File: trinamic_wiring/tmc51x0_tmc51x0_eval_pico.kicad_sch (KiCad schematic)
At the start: 4 parts, among them M1 Stepper_Motor

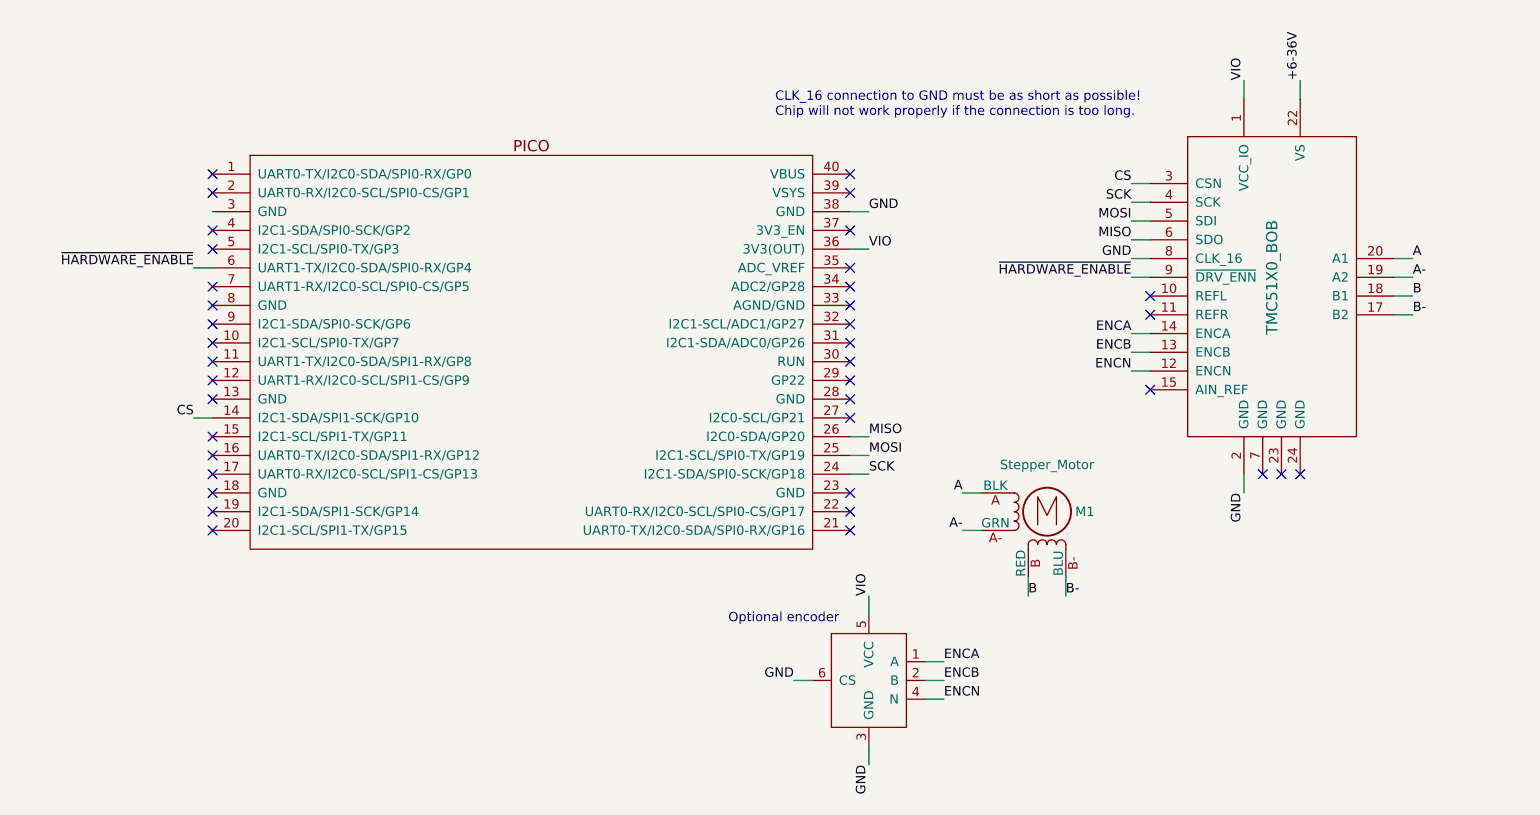
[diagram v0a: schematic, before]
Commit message: Add eval board
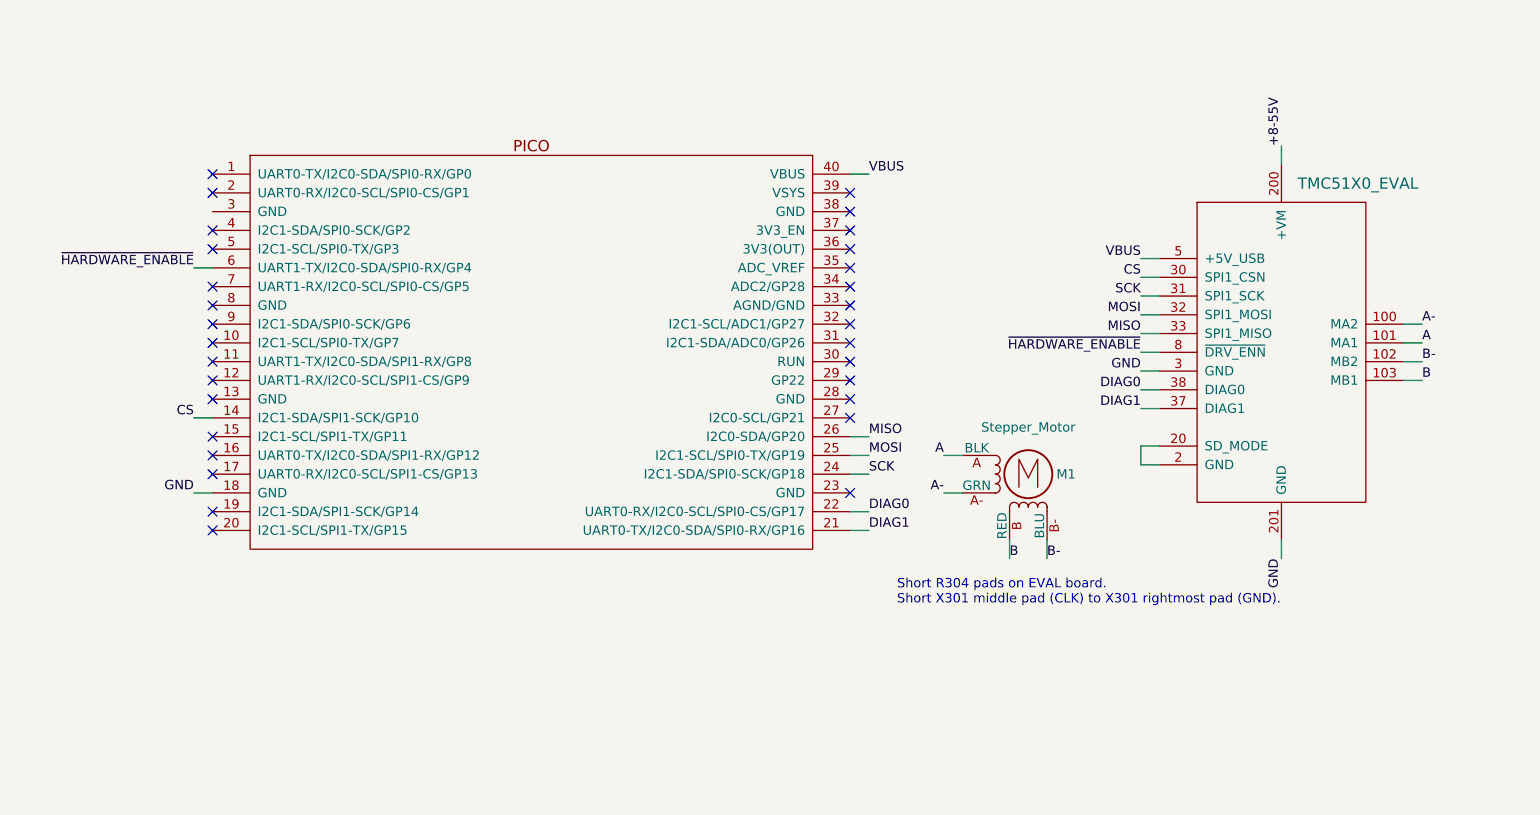
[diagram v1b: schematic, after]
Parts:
- removed BOB1: TMC51X0_BOB, symbol Janelia:TMC51X0_BOB
- removed ENC1: ENCODER_EMS22Q, symbol Janelia:ENCODER_EMS22Q
- added EVAL1: TMC51X0_EVAL, symbol Janelia:TMC51X0_EVAL
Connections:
- net A: now also EVAL1.101 (MA1)
- net A-: now also EVAL1.100 (MA2)
- net B: now also EVAL1.103 (MB1)
- net B-: now also EVAL1.102 (MB2)
- net CS: now also EVAL1.30 (SPI1_CSN)
- net GND: now also A3.18 (GND), EVAL1.201 (GND), EVAL1.3 (GND); no longer A3.38 (GND)
- net MISO: now also EVAL1.33 (SPI1_MISO)
- net MOSI: now also EVAL1.32 (SPI1_MOSI)
- net SCK: now also EVAL1.31 (SPI1_SCK)
- net ~{HARDWARE_ENABLE}: now also EVAL1.8 (~{DRV_ENN})
- net DIAG1: now reaches A3.21 (UART0-TX/I2C0-SDA/SPI0-RX/GP16)
- net DIAG1: now also EVAL1.37 (DIAG1)
- net DIAG0: now reaches A3.22 (UART0-RX/I2C0-SCL/SPI0-CS/GP17)
- net DIAG0: now also EVAL1.38 (DIAG0)
- net VBUS: now reaches A3.40 (VBUS)
- net VBUS: now also EVAL1.5 (+5V_USB)
- net VIO: no longer names the net of A3.36 (3V3(OUT))
- new net: EVAL1.2 (GND), EVAL1.20 (SD_MODE)
- new net +8-55V: EVAL1.200 (+VM)
- no-connect marks 38 -> 30
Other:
- note added: "Short R304 pads on EVAL board. Short X301 middle pad (CLK) to X301 rightmost pad (GND)."
- note removed: "CLK_16 connection to GND must be as short as possible! Chip will not work properly if the connection is too long."
- note removed: "Optional encoder"
- moved on the sheet: M1

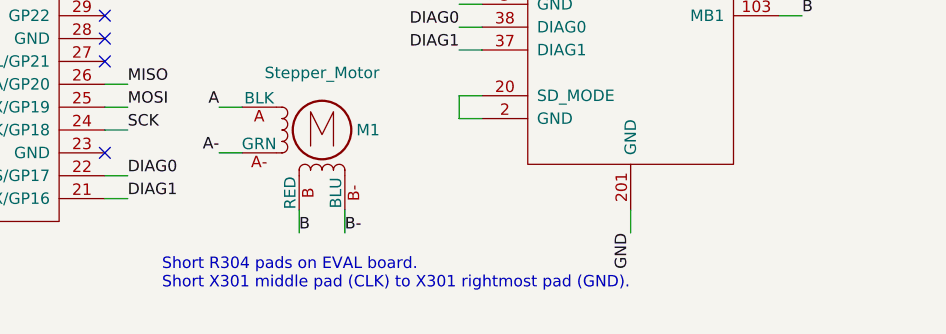
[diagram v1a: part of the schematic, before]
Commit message: Deleted sheet and updated comment on another
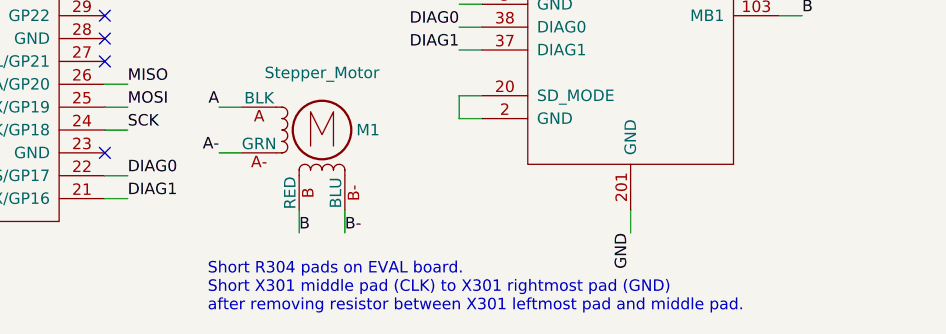
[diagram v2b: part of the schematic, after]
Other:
- note added: "Short R304 pads on EVAL board. Short X301 middle pad (CLK) to X301 rightmost pad (GND) after removing resistor between X301 leftmost pad and middle pad."
- note removed: "Short R304 pads on EVAL board. Short X301 middle pad (CLK) to X301 rightmost pad (GND)."
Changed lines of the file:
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@@
     (stroke (width 0) (type default))
   )
-  (text "Short R304 pads on EVAL board.\nShort X301 middle pad (CLK) to X301 rightmost pad (GND). "
-    (at 129.54 146.05 0)
+  (text "Short R304 pads on EVAL board.\nShort X301 middle pad (CLK) to X301 rightmost pad (GND)\nafter removing resistor between X301 leftmost pad and middle pad. "
+    (at 134.62 148.59 0)
     (effects (font (size 1.27 1.27)) (justify left bottom))
   )

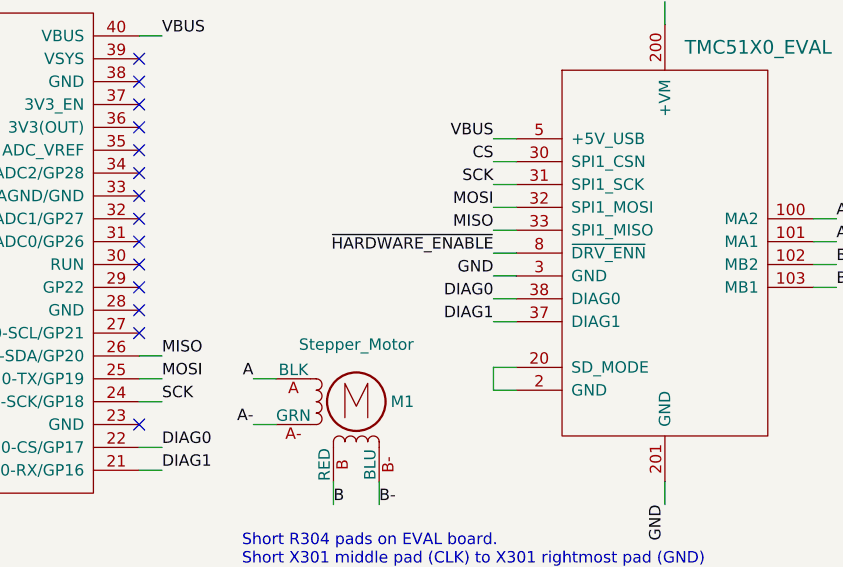
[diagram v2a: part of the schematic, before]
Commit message: miso -> cipo, mosi -> copi
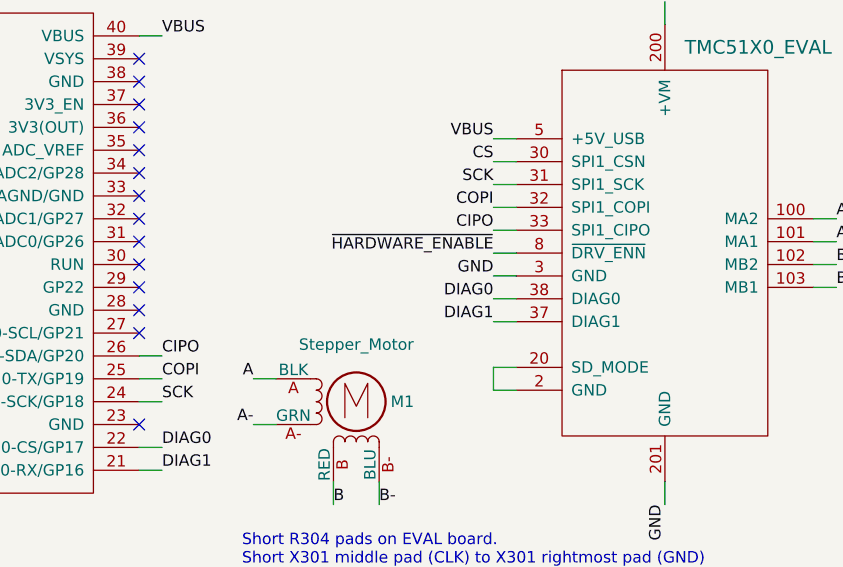
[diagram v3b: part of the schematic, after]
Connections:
- net MISO renamed CIPO
- net MOSI renamed COPI
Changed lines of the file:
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@@
     (effects (font (size 1.27 1.27)) (justify left bottom))
   )
-  (label "MISO" (at 162.56 109.22 180) (fields_autoplaced)
+  (label "CIPO" (at 162.56 109.22 180) (fields_autoplaced)
     (effects (font (size 1.27 1.27)) (justify right bottom))
   )
@@
     (effects (font (size 1.27 1.27)) (justify right bottom))
   )
-  (label "MOSI" (at 162.56 106.68 180) (fields_autoplaced)
+  (label "COPI" (at 162.56 106.68 180) (fields_autoplaced)
     (effects (font (size 1.27 1.27)) (justify right bottom))
   )
@@
     (effects (font (size 1.27 1.27)) (justify left bottom))
   )
-  (label "MISO" (at 125.73 123.19 0) (fields_autoplaced)
+  (label "CIPO" (at 125.73 123.19 0) (fields_autoplaced)
     (effects (font (size 1.27 1.27)) (justify left bottom))
   )
@@
     (effects (font (size 1.27 1.27)) (justify right bottom))
   )
-  (label "MOSI" (at 125.73 125.73 0) (fields_autoplaced)
+  (label "COPI" (at 125.73 125.73 0) (fields_autoplaced)
     (effects (font (size 1.27 1.27)) (justify left bottom))
   )
